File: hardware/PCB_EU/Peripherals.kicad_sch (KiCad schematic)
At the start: 18 parts, among them J301 MEM2061 SPI, U301 MCP7940N-I/SN, Y301 32.768k CL7p

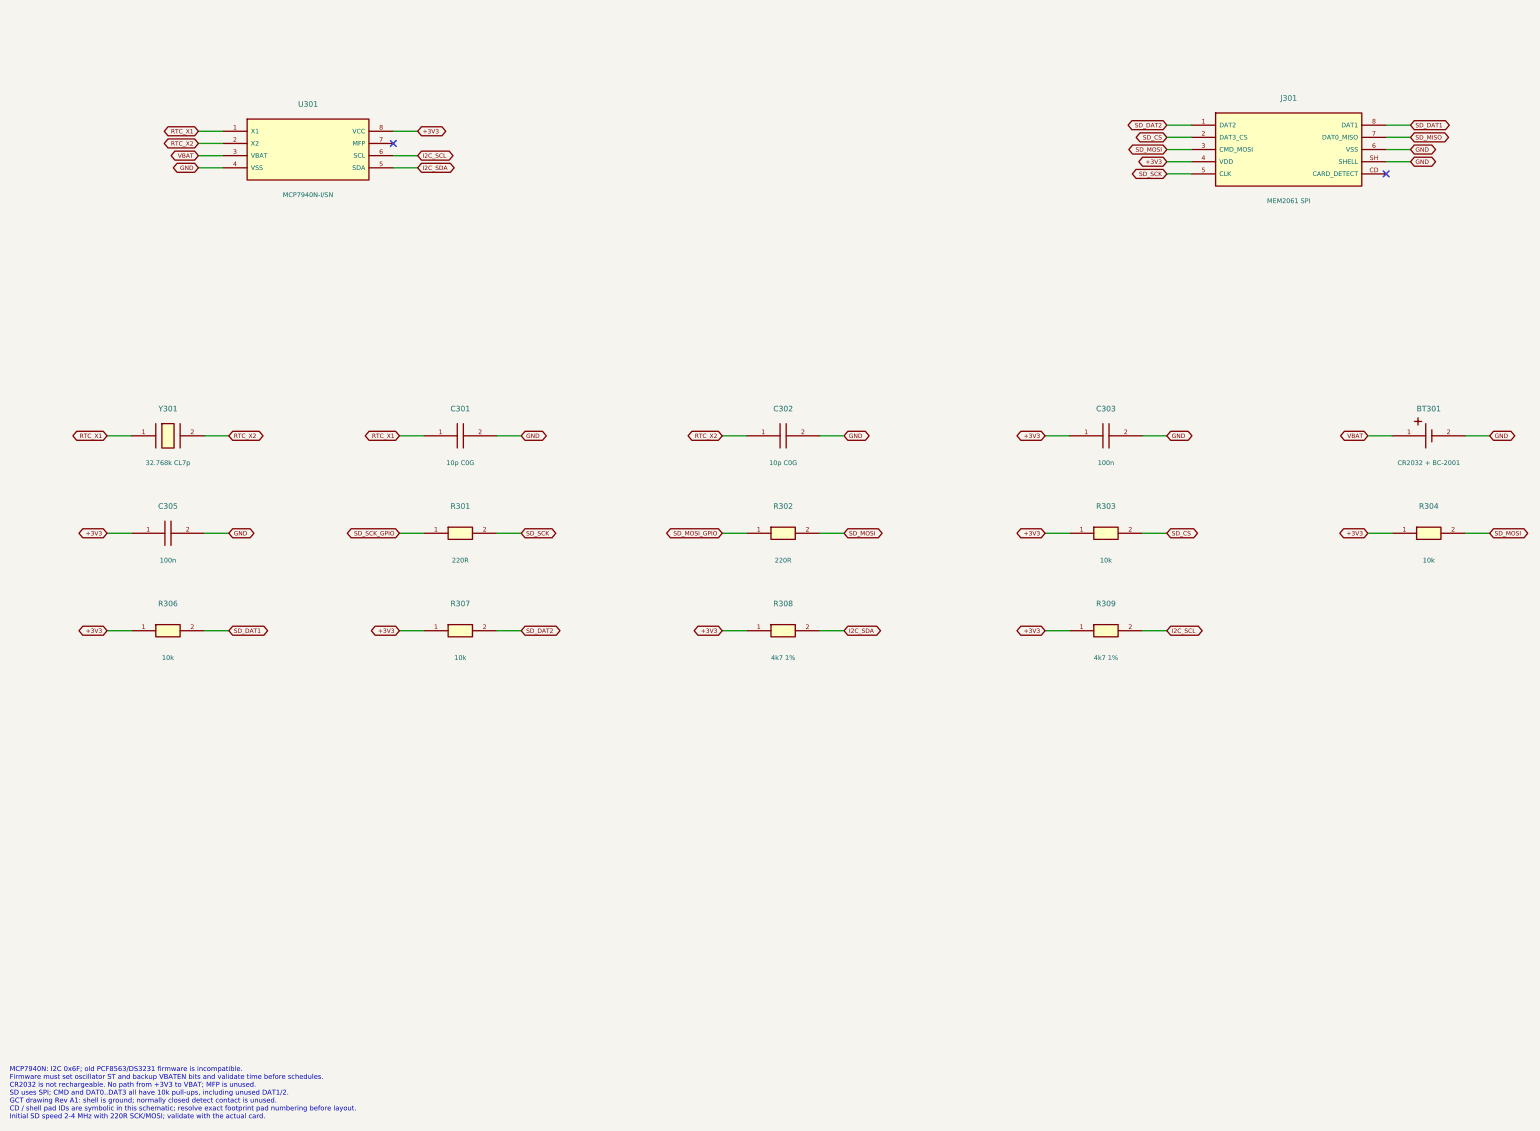
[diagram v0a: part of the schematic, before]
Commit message: hardware: complete EU mechanical footprint assignments and validate pad maps
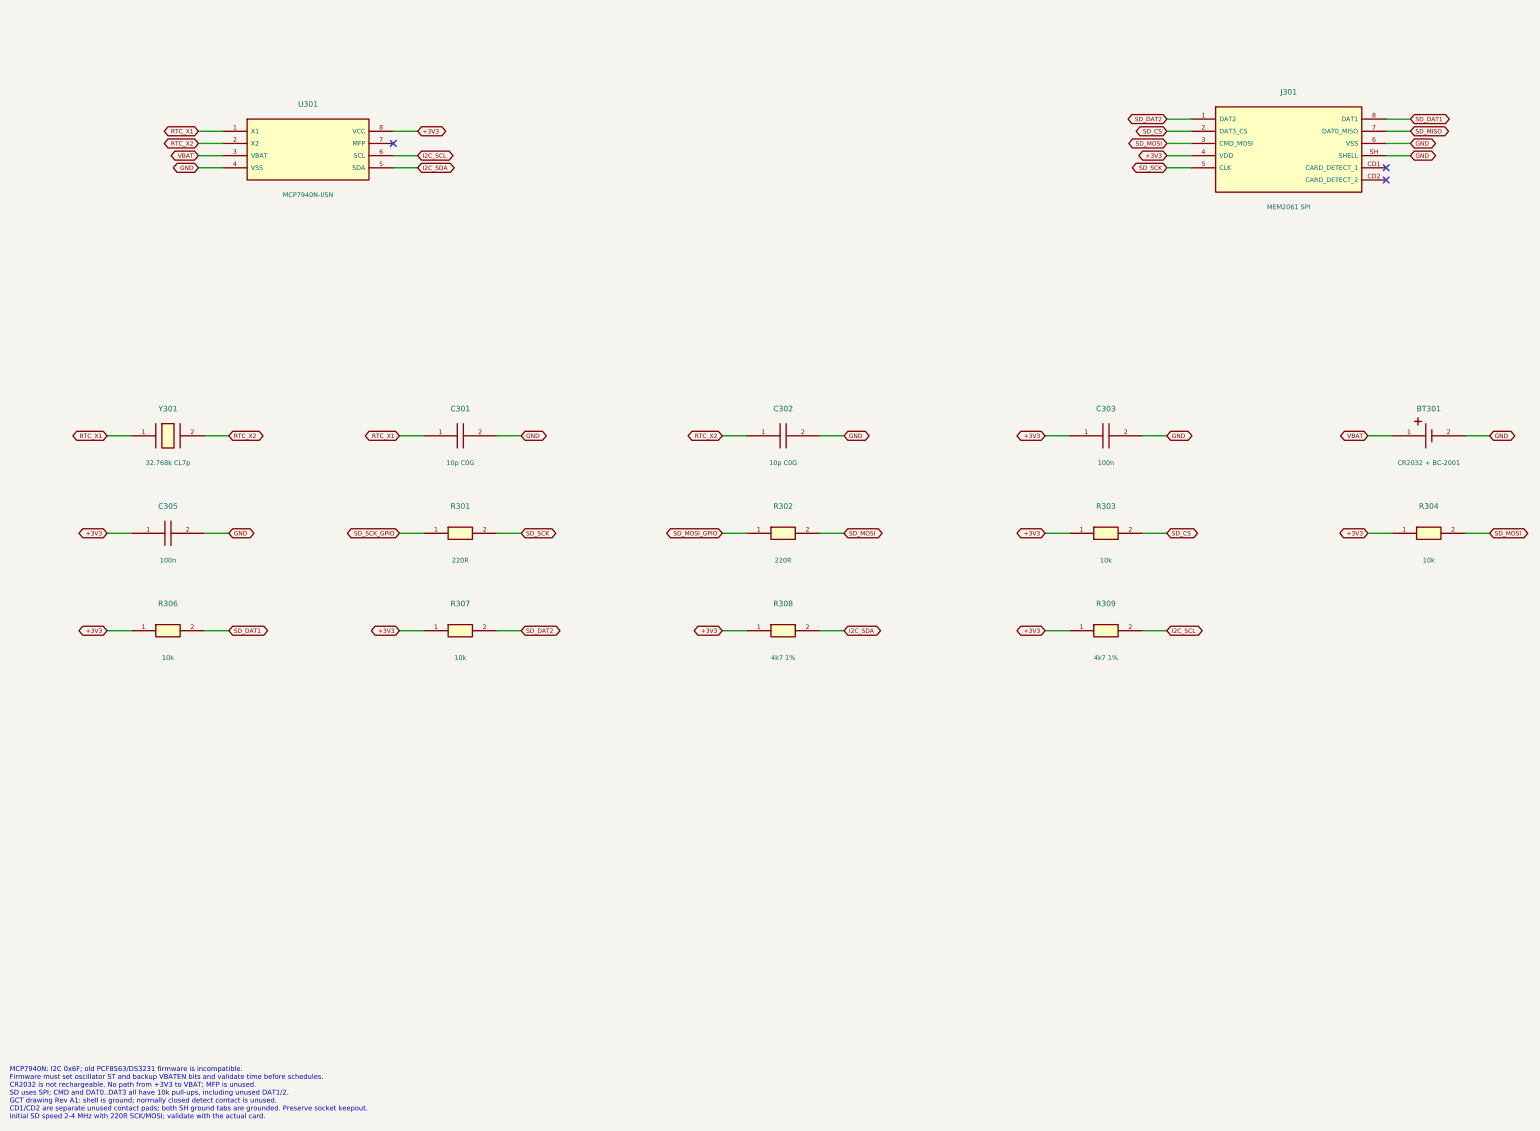
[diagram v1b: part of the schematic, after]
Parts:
- BT301: footprint (none) -> EU_Mechanical:Battery_COMF_BC-2001; Design_note BC-2001 clip footprint / negative PCB contact still pending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 -> COMF BC-2001: side pads 1 positive; centre pad 2 negative, 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; FootprintStatus PENDING - no approved footprint -> DRAWING CHECKED - physical fit and PCB validation pending
- J301: footprint (none) -> EU_Mechanical:microSD_GCT_MEM2061-01-188-00-A; Design_note GCT MEM2061 drawing A1, no locating pegs, normally closed CD -> GCT MEM2061 A1: without pegs; separate CD1/CD2 pads unused;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; FootprintStatus PENDING - no approved footprint -> DRAWING CHECKED - physical fit and PCB validation pending
- Y301: footprint (none) -> EU_Mechanical:Crystal_Abracon_ABS07; FootprintStatus PENDING - no approved footprint -> DRAWING CHECKED - physical fit and PCB validation pending
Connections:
- no-connect marks 2 -> 3
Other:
- note added: "MCP7940N: I2C 0x6F; old PCF8563/DS3231 firmware is incompatible. Firmware must set oscillator ST and backup VBATEN bits and validate time before schedules. CR2032 is not rechargeable. No path from +3V3 to VBAT; MFP is unused. SD uses SPI; CMD and DAT0..DAT3 all have 10k pull-ups, including unused DAT1/2. GCT drawing Rev A1: shell is ground; normally closed detect contact is unused. CD1/CD2 are se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"
- note removed: "MCP7940N: I2C 0x6F; old PCF8563/DS3231 firmware is incompatible. Firmware must set oscillator ST and backup VBATEN bits and validate time before schedules. CR2032 is not rechargeable. No path from +3V3 to VBAT; MFP is unused. SD uses SPI; CMD and DAT0..DAT3 all have 10k pull-ups, including unused DAT1/2. GCT drawing Rev A1: shell is ground; normally closed detect contact is unused. CD / shell pad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"
